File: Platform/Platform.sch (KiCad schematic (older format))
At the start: 0 parts

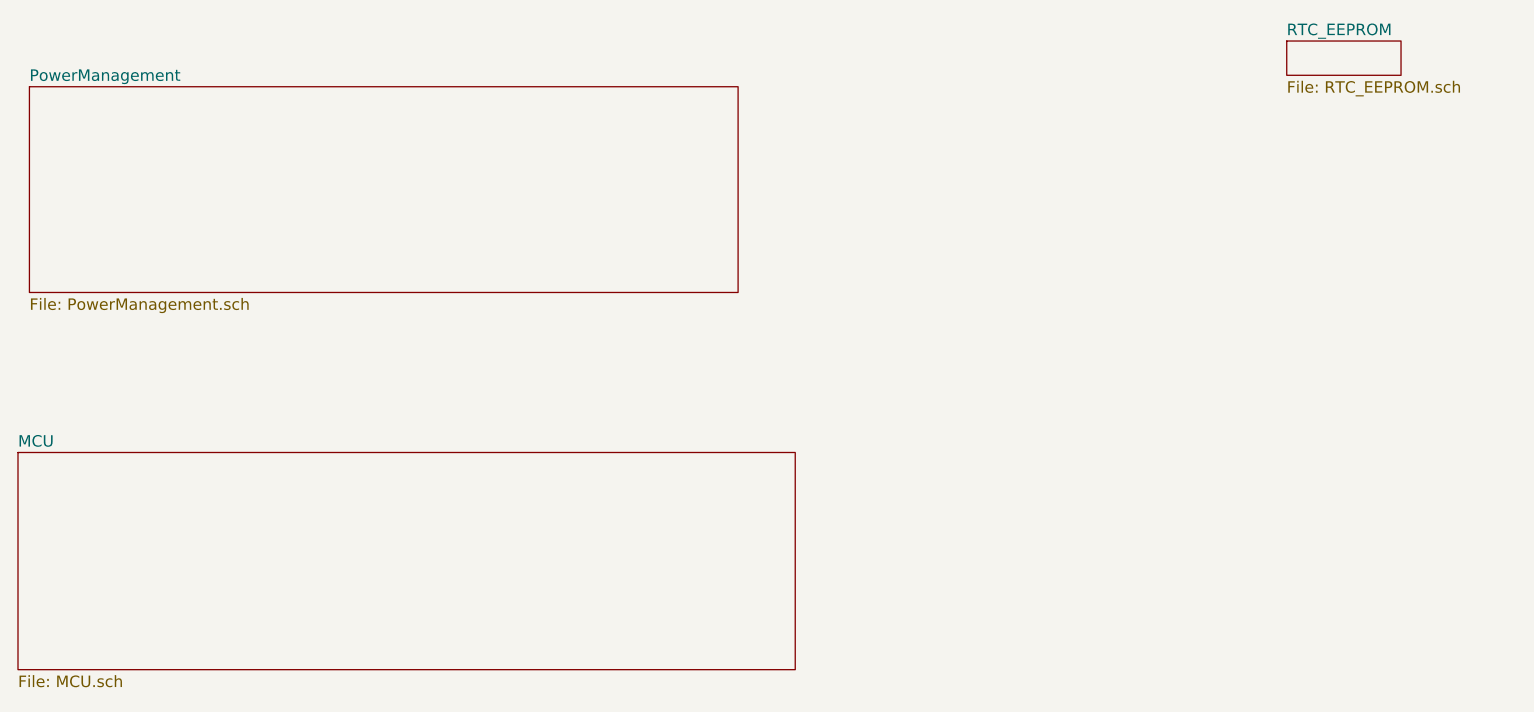
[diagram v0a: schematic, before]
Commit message: Added RTC and EEPROM
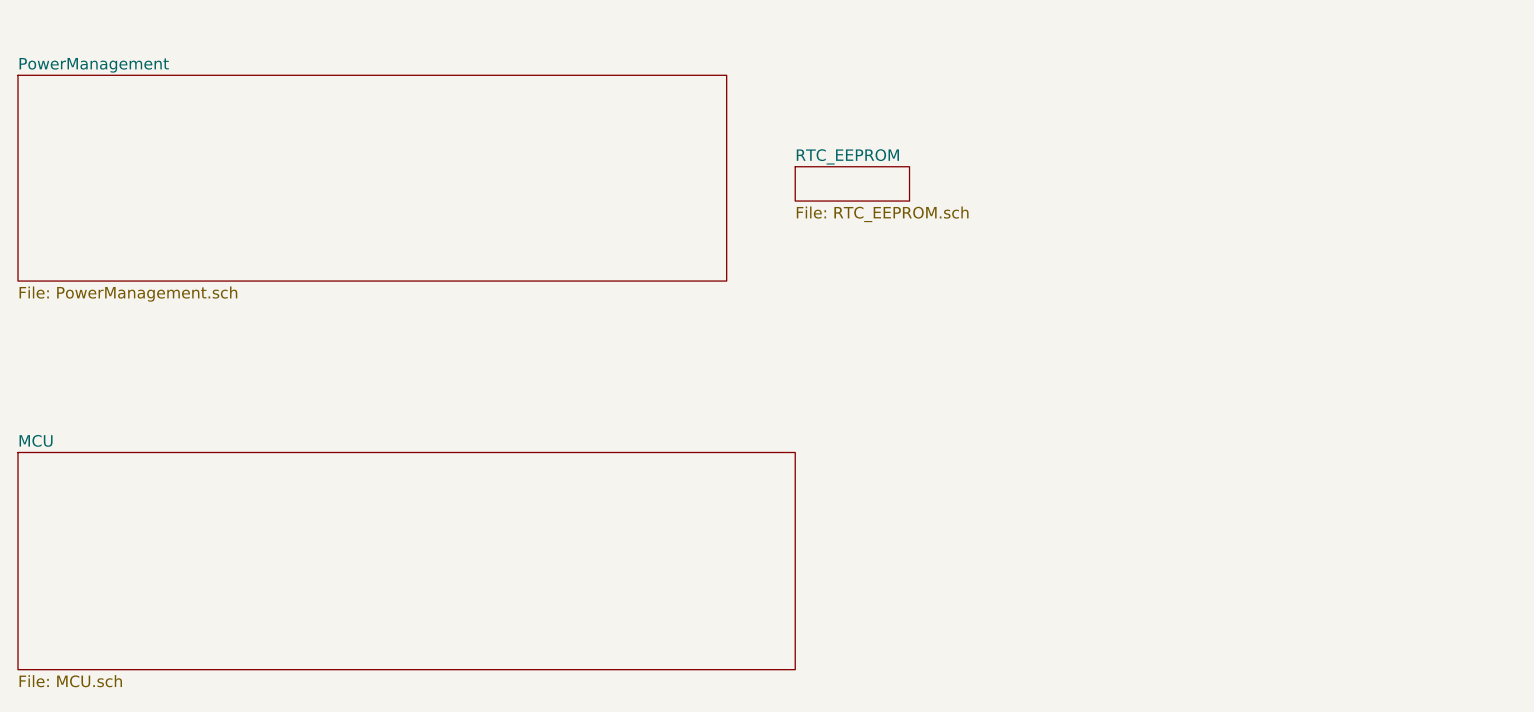
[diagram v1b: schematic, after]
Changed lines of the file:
@@
 $EndDescr
 $Sheet
-S 2150 2650 3100 900
+S 2100 2600 3100 900
 U 5FB6B30F
 F0 "PowerManagement" 50
@@
 $EndSheet
 $Sheet
-S 7650 2450 500  150
+S 5500 3000 500  150
 U 5FB03683
 F0 "RTC_EEPROM" 50
